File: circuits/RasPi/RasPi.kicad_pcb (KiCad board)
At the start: 2 copper layers, 90 x 57 mm, 276 parts, among them J1 Conn_01x14_Pin, J12 Conn_01x02_MountingPin, J13 Conn_01x03_MountingPin, J14 Conn_01x02_MountingPin, J15 USB_C_Receptacle_USB2.0, J2 Conn_01x06_MountingPin, J3 Conn_01x06_MountingPin, J5 Conn_01x05_Pin, J6 Conn_01x03_MountingPin, J7 RJ45_Hanrun_HR911105A_Horizon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, J8 Conn_01x07_MountingPin, J9 Conn_01x04_MountingPin, Q1 S8550, Q10 BSS138, Q12 SSM6J808R, Q13 BSS138, Q14 SSM6J808R, Q15 S8550, Q16 SSM3J332R, Q17 S8550, Q18 S8550, Q19 S8550, Q2 S8550, Q20 BSS138, Q21 BSS138, Q22 S8550, Q23 BSS138, Q25 BSS138, Q26 SSM3J332R, Q27 BSS138, Q28 SSM3J332R, Q29 BSS138, Q3 S8550, Q30 BSS138, Q33 BSS138, Q4 S8550, Q5 S8550, Q6 SSM3J332R, Q7 S8550, Q8 SSM3J332R, Q9 S8550, SW1 SW_SPST, SW2 SW_DIP_x04, SW3 SW_SPDT, SW4 SW_SPDT_White, SW5 SW_SPDT, SW6 SW_SPDT, SW7 SW_SPST, U1 STM32F446RETx, U10 MAX3485, U11 MAX3485, U12 MAX3485, U13 TPS54560BDDA, U14 MAX3485, U15 STM32H723VGTx, U16 AZ1117CH-3.3, U17 M51957B, U18 DAC_PT8211S, U19 DCDC_TPS61023, U2 MAX3485, U20 FT231XS, U3 MAX3485, U4 MAX3485, U5 MAX3485, U6 SBC_RPi-CM4, U7 FPGA_TangPrimer25K_Core, U8 MAX3485, U9 MAX3485, Y1 16MHz

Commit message: 更新
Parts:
- removed C10: 1uF, Capacitor_SMD:C_0402_1005Metric
- removed C9: 4.7uF, Capacitor_SMD:C_0603_1608Metric
- removed J15: USB_C_Receptacle_USB2.0, Connector_USB:USB_C_Receptacle_G-Switch_GT-USB-7010ASV
- removed L2, L4: 2.2uH, MyLibrary:Inductor_CDPH4D19F
- removed Q29, Q30, Q33: BSS138, Package_TO_SOT_SMD:SOT-23
- removed R3: 10k, Resistor_SMD:R_0402_1005Metric
- removed U20: FT231XS, Package_SO:SSOP-20_3.9x8.7mm_P0.635mm
- added C19: 2.2uF, Capacitor_SMD:C_0402_1005Metric, B.Cu at (-0.40, -13.3)
- added C62: 2.2uF, Capacitor_SMD:C_0402_1005Metric, B.Cu at (14.3, -18.0)
- added C63: 1uF, Capacitor_SMD:C_0402_1005Metric, B.Cu at (5.70, 1.40)
- added J10: USB_C_Receptacle_USB2.0_16P, Connector_USB:USB_C_Receptacle_G-Switch_GT-USB-7010ASV, B.Cu at (40.2, 16.4)
- added J11: Micro_SD_Card_Det_Hirose_DM3AT, TomoshibiLibrary:Connector_SDCard_DM3AT, B.Cu at (-3.39, 17.5)
- added J4: Conn_01x02_Pin, Connector_JST:JST_XH_B2B-XH-AM_1x02_P2.50mm_Vertical, F.Cu at (23.7, 1.80)
- added Q11: 2N7002, Package_TO_SOT_SMD:SOT-23, B.Cu at (68.1, 33.7)
- added Q24: 2N7002, Package_TO_SOT_SMD:SOT-23, B.Cu at (-22.7, 46.9)
- C1, C11, C12, C13, C14, C15, C16, C17, C18, C2, C20, C21, C23, C24, C25, C26, C28, C3, C30, C31, C33, C35, C36, C37, C38, C39, C4, C40, C41, C42, C43, C44, C45, C46, C47, C49, C5, C50, C51, C52, C53, C54, C55, C56, C57, C6, C7, C8, D1, D16, D17, D18, D27, D4, D5, D6, D8, J12, J14, J2, J6, J8, J9, Q1, Q15, Q17, Q18, Q19, Q2, Q22, Q26, Q28, Q3, Q4, Q5, Q6, Q7, Q8, Q9, R1, R10, R102, R103, R104, R105, R106, R107, R108, R109, R11, R110, R111, R112, R113, R114, R117, R119, R12, R120, R121, R122, R13, R14, R15, R16, R17, R18, R19, R2, R20, R21, R22, R23, R24, R25, R26, R27, R28, R29, R30, R31, R32, R33, R34, R35, R36, R37, R38, R39, R4, R40, R41, R44, R45, R46, R47, R48, R49, R5, R50, R53, R54, R55, R56, R57, R58, R59, R6, R60, R61, R62, R63, R64, R65, R66, R67, R68, R69, R7, R70, R71, R72, R73, R74, R75, R76, R77, R78, R79, R8, R80, R81, R82, R83, R84, R85, R86, R87, R88, R89, R9, R90, R91, R92, R93, R94, R95, R96, R97, R98, U10, U11, U12, U13, U14, U15, U16, U17, U18, U19, U2, U3, U4, U5, U8, U9, Y1: moved to B.Cu
- C22: value 1uF -> 0.1uF; moved to B.Cu
- J7: value RJ45_Hanrun_HR911105A_Horizontal -> RJ45_LPJK7001AGNL
- L1: value 22uH -> 1uH; footprint TomoshibiLibrary:Inductor_CDPH4D19F -> Inductor_SMD:L_0603_1608Metric; moved to B.Cu
- Q10, Q13, Q20, Q21, Q23, Q25, Q27: value BSS138 -> 2N7002; moved to B.Cu
- Q12, Q14: footprint TomoshibiLibrary:Package_TSOP6F -> Package_SO:TSOP-6_1.65x3.05mm_P0.95mm
- Q16: value SSM3J332R -> SSM6J808R; footprint Package_TO_SOT_SMD:SOT-23W -> Package_SO:TSOP-6_1.65x3.05mm_P0.95mm; moved to B.Cu
- R100: value 10k -> 1.8k; footprint Resistor_SMD:R_0402_1005Metric -> Resistor_SMD:R_0603_1608Metric; moved to B.Cu
- R99: value 53.6k -> 13k; footprint Resistor_SMD:R_0402_1005Metric -> Resistor_SMD:R_0603_1608Metric; moved to B.Cu
- SW3, SW6: footprint TomoshibiLibrary:SW_Slide_3P_SPDT -> TomoshibiLibrary:SW_Slide_SPDT_SSSS213202
- SW4: value SW_SPDT_White -> SW_SPDT
- U1: value STM32F446RETx -> MODULE_SC0678; footprint Package_QFP:LQFP-64_10x10mm_P0.5mm -> TomoshibiLibrary:SBC_RPi-CM4
- U6: value SBC_RPi-CM4 -> FT231XS; footprint MyLibrary:SBC_RPi-CM4 -> Package_SO:SSOP-20_3.9x8.7mm_P0.635mm
- moved C54 347.9 mm to (-72.3, -32.0)
- moved C53 347.7 mm to (-72.2, -30.2)
- moved U18 347.6 mm to (-70.1, -35.6), turned to 180 degrees
- moved Q21 345.5 mm to (-65.3, 35.7), turned to 180 degrees
- moved R89 341.3 mm to (-62.9, 35.7), turned to -90 degrees
- moved C15 334.7 mm to (-59.4, 35.6), turned to 180 degrees
- moved C16 334.4 mm to (-59.4, 36.6), turned to 180 degrees
- moved C17 334.1 mm to (-59.4, 37.6), turned to 180 degrees
- moved C18 333.8 mm to (-59.4, 38.6), turned to 180 degrees
- moved C26 333.5 mm to (-59.4, 39.6), turned to 180 degrees
- moved R84 328.1 mm to (-46.3, 24.6), turned to 180 degrees
- moved J8 327.8 mm to (-42.4, -3.20), turned to 90 degrees
- moved D23 319.8 mm to (-25.7, 45.0)
- moved D24 318.3 mm to (-25.7, 39.0)
- moved D25 318.1 mm to (-25.7, 40.5)
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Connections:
- net /RingNW/F446RXx_RS485XTX renamed /RingNW/H723RXx_RS485XTX
- net /RingNW/F446RXx_RS485YTX renamed /RingNW/H723RXx_RS485YTX
- net /RingNW/F446TXx_RS485XRX renamed /RingNW/H723TXx_RS485XRX
- net /RingNW/F446TXx_RS485YRX renamed /RingNW/H723TXx_RS485YRX
- C20 pad 1: Net-(C20-Pad1) -> +3.3V
- C22 pad 1: GND -> +3.3V
- C22 pad 2: +3.3V -> GND
- C58 pad 2: GND -> Net-(J10-SHIELD)
- C59 pad 2: GND -> Net-(J10-SHIELD)
- C60 pad 1: GND -> Net-(J10-SHIELD)
- C60 pad 2: Net-(U20-3V3OUT) -> Net-(U6-3V3OUT)
- Q10 pad 1: Net-(D16-K) -> /RingNW/LED_nR0
- Q10 pad 2: Net-(Q10-S) -> GND
- Q10 pad 3: /Power/VSYS -> Net-(D20-A)
- Q13 pad 1: /Power/PowerSW -> /F446RE->RasPi_GPIO3
- Q13 pad 3: Net-(Q13-D) -> /RasPi_GPIO3
- Q16 pad 1: Net-(Q16-G) -> +5V
- Q16 pad 3: /Power/VSYS -> Net-(Q16-G)
- Q20 pad 1: /F446RE->RasPi_GPIO3 -> /ResetIC->RasPi_SHDN
- Q20 pad 3: /RasPi_GPIO3 -> /RasPi_SHDN
- Q23 pad 1: /ResetIC->RasPi_SHDN -> /RasPi_CM4/LED_nR0
- Q23 pad 3: /RasPi_SHDN -> Net-(D29-A)
- R101 pad 1: Net-(U20-USBDP) -> Net-(U6-USBDP)
- R115 pad 1: Net-(U20-USBDM) -> Net-(U6-USBDM)
- R2 pad 1: /RingNW/BOOT -> /RingNW/BOOT0
- R45 pad 1: Net-(Q10-S) -> unconnected-(R45-Pad1)
- R51 pad 1: GND -> Net-(J10-SHIELD)
- R52 pad 1: GND -> Net-(J10-SHIELD)
- R61 pad 2: Net-(Q13-D) -> Net-(Q11-D)
- SW5 pad 1: /RasPi_CM4/GLOBAL_EN -> unconnected-(SW5-A-Pad1)
- SW5 pad 3: unconnected-(SW5-C-Pad3) -> /RasPi_CM4/GLOBAL_EN
- U1 pad 1: +3.3V -> GND
- U1 pad 10: unconnected-(U1-PC2-Pad10) -> /RasPi_CM4/TRD0_N
- U1 pad 12: GND -> /RasPi_CM4/TRD0_P
- U1 pad 13: +3.3V -> GND
- U1 pad 14: unconnected-(U1-PA0-Pad14) -> GND
- U1 pad 15: unconnected-(U1-PA1-Pad15) -> /RasPi_CM4/ETH_LEDY
- U1 pad 17: unconnected-(U1-PA3-Pad17) -> /RasPi_CM4/ETH_LEDG
- U1 pad 18: GND -> unconnected-(U1A-ETHERNET_SYNC_OUT-Pad18)
- U1 pad 19: +3.3V -> unconnected-(U1A-ETHERNET_~{LED1}-Pad19)
- U1 pad 2: unconnected-(U1-PC13-Pad2) -> GND
- U1 pad 21: unconnected-(U1-PA5-Pad21) -> /RasPi_CM4/LED_nACT
- U1 pad 22: unconnected-(U1-PA6-Pad22) -> GND
- U1 pad 23: unconnected-(U1-PA7-Pad23) -> GND
- U1 pad 25: unconnected-(U1-PC5-Pad25) -> /PCM_DOUT
- U1 pad 26: unconnected-(U1-PB0-Pad26) -> /PCM_FS
- U1 pad 27: unconnected-(U1-PB1-Pad27) -> /PCM_DIN
- U1 pad 28: Net-(U1-PB2) -> unconnected-(U1A-GPIO13-Pad28)
- U1 pad 30: Net-(U1-VCAP_1) -> unconnected-(U1A-GPIO6-Pad30)
- U1 pad 31: GND -> unconnected-(U1A-GPIO12-Pad31)
- U1 pad 32: +3.3V -> GND
- U1 pad 33: unconnected-(U1-PB12-Pad33) -> GND
- U1 pad 4: unconnected-(U1-PC15-Pad4) -> /RasPi_CM4/TRD1_P
- U1 pad 42: unconnected-(U1-PA9-Pad42) -> GND
- U1 pad 43: unconnected-(U1-PA10-Pad43) -> GND
- U1 pad 46: /RingNW/SWDIO -> unconnected-(U1A-GPIO22-Pad46)
- U1 pad 47: GND -> unconnected-(U1A-GPIO23-Pad47)
- U1 pad 48: +3.3V -> unconnected-(U1A-GPIO27-Pad48)
- U1 pad 49: /RingNW/SWCLK -> /PCM_CLK
- U1 pad 5: /RingNW/HSE_IN -> unconnected-(U1A-ETHERNET_PAIR3_N-Pad5)
- U1 pad 51: unconnected-(U1-PC10-Pad51) -> /RasPi_CM4/RasPiRX0_SerialTX
- U1 pad 52: unconnected-(U1-PC11-Pad52) -> GND
- U1 pad 53: unconnected-(U1-PC12-Pad53) -> GND
- U1 pad 55: /RingNW/SWO -> /RasPi_CM4/RasPiTX0_SerialRX
- U1 pad 56: unconnected-(U1-PB4-Pad56) -> /RasPi_GPIO3
- U1 pad 57: unconnected-(U1-PB5-Pad57) -> /RasPi_CM4/SD_CLK
- U1 pad 59: unconnected-(U1-PB7-Pad59) -> GND
- U1 pad 6: /RingNW/HSE_OUT -> /RasPi_CM4/TRD1_N
- U1 pad 60: /RingNW/BOOT -> GND
- U1 pad 61: unconnected-(U1-PB8-Pad61) -> /RasPi_CM4/SD_DAT3
- U1 pad 62: unconnected-(U1-PB9-Pad62) -> /RasPi_CM4/SD_CMD
- U1 pad 63: GND -> /RasPi_CM4/SD_DAT0
- U1 pad 64: +3.3V -> unconnected-(U1A-SD_DAT5-Pad64)
- U1 pad 7: /RingNW/NRST -> GND
- U1 pad 8: unconnected-(U1-PC0-Pad8) -> GND
- U15 pad 20: unconnected-(U15-VREF+-Pad20) -> +3.3V
- U15 pad 48: unconnected-(U15-VCAP-Pad48) -> Net-(C19-Pad1)
- U15 pad 72: unconnected-(U15-PA13(JTMS-Pad72) -> /RingNW/SWDIO
- U15 pad 73: Net-(C20-Pad1) -> Net-(C62-Pad1)
- U15 pad 76: unconnected-(U15-PA14(JTCK-Pad76) -> /RingNW/SWCLK
- U15 pad 89: unconnected-(U15-PB3(JTDO-Pad89) -> /RingNW/SWO
- U15 pad 94: /RingNW/BOOT -> /RingNW/BOOT0
- U6 pad 1: GND -> unconnected-(U6-~{DTR}-Pad1)
- U6 pad 11: unconnected-(U6A-ETHERNET_PAIR2_P-Pad11) -> Net-(U6-USBDP)
- U6 pad 12: unconnected-(U6A-ETHERNET_PAIR0_P-Pad12) -> Net-(U6-USBDM)
- U6 pad 13: GND -> Net-(U6-3V3OUT)
- U6 pad 14: GND -> Net-(U6-3V3OUT)
- U6 pad 15: unconnected-(U6A-ETHERNET_~{LED3}-Pad15) -> VBUS
- U6 pad 16: unconnected-(U6A-ETHERNET_SYNC_IN-Pad16) -> GND
- U6 pad 2: GND -> unconnected-(U6-~{RTS}-Pad2)
- U6 pad 20: unconnected-(U6A-EEPROM_~{WP}-Pad20) -> /RasPi_CM4/RasPiRX0_SerialTX
- U6 pad 3: unconnected-(U6A-ETHERNET_PAIR3_P-Pad3) -> Net-(U6-3V3OUT)
- U6 pad 4: unconnected-(U6A-ETHERNET_PAIR1_P-Pad4) -> /RasPi_CM4/RasPiTX0_SerialRX
- U6 pad 6: unconnected-(U6A-ETHERNET_PAIR1_N-Pad6) -> Net-(J10-SHIELD)
- U6 pad 7: GND -> unconnected-(U6-~{DSR}-Pad7)
- U6 pad 8: GND -> unconnected-(U6-~{DCD}-Pad8)
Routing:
- net /RasPi_CM4/TRD1_N: track 0.00 -> 55.1 mm
- net /RasPi_CM4/TRD1_P: track 0.00 -> 55.0 mm
- net /RasPi_CM4/TRD0_P: track 0.00 -> 51.3 mm
- net /RasPi_CM4/TRD0_N: track 0.00 -> 51.3 mm
- net unconnected-(U7-B10_IOL12B-PadB57): track 0.00 -> 45.8 mm
- net unconnected-(U7-B11_IOL12A-PadB55): track 0.00 -> 44.4 mm
- net unconnected-(U7-C11_IOL5A-PadB51): track 0.00 -> 41.8 mm
- net +3.3V: track 0.00 -> 28.6 mm
- net /FPGA_TangPrimerCore/RS485_Panel/RS485_Panel0: track 0.00 -> 26.4 mm
- net /FPGA_TangPrimerCore/RS485_Panel/RS485_Panel1: track 0.00 -> 22.2 mm
- net /DSI_D1_P: track 0.00 -> 21.4 mm, vias 0 -> 2
- net /DSI_D1_N: track 0.00 -> 21.4 mm, vias 0 -> 2
- net /DSI_D0_P: track 0.00 -> 21.3 mm, vias 0 -> 2
- net /DSI_CK_N: track 0.00 -> 21.2 mm, vias 0 -> 2
- net /DSI_D0_N: track 0.00 -> 21.2 mm, vias 0 -> 2
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- added copper zone on In1.Cu, net GND
- added copper zone on In2.Cu, net GND
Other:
- outline, holes or cut-outs redrawn
- copper layers 2 -> 4
- board text added: "3.3V"
- board text added: "5VDCDC"
- board text added: "表：放電 裏：昇圧"

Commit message: raspi基板回路図
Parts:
- removed J8: Conn_01x07_MountingPin, Connector_Molex:Molex_PicoBlade_53261-0771_1x07-1MP_P1.25mm_Horizontal
- added C10: 10uF, Capacitor_SMD:C_1206_3216Metric, B.Cu at (53.5, 13.7)
- added C64: 22uF, Capacitor_SMD:C_0805_2012Metric, F.Cu at (64.5, 55.8)
- added C65: 4.7nF, Capacitor_SMD:C_0402_1005Metric, F.Cu at (64.3, 48.6)
- added C66: 100uF, Capacitor_SMD:C_1206_3216Metric, F.Cu at (64.3, 51.1)
- added C67: 100uF, Capacitor_SMD:C_1206_3216Metric, F.Cu at (-40.8, 49.8)
- added C68: 10uF, Capacitor_SMD:C_0805_2012Metric, F.Cu at (-35.7, 54.2)
- added C70: 15pF, Capacitor_SMD:C_0402_1005Metric, F.Cu at (-31.3, 49.1)
- added C9: 100uF, Capacitor_SMD:C_1206_3216Metric, B.Cu at (53.1, 26.6)
- added D19: Blue, LED_SMD:LED_0603_1608Metric_Pad1.05x0.95mm_HandSolder, F.Cu at (22.7, -18.2)
- added D28: Blue, LED_SMD:LED_0603_1608Metric_Pad1.05x0.95mm_HandSolder, F.Cu at (22.7, -16.7)
- added H1: MountingHole_Pad, TestPoint:TestPoint_Pad_1.0x1.0mm, F.Cu at (-40.4, -3.50)
- added H2: MountingHole_Pad, TestPoint:TestPoint_Pad_1.0x1.0mm, F.Cu at (-40.4, -1.90)
- added H3: MountingHole_Pad, TestPoint:TestPoint_Pad_1.0x1.0mm, F.Cu at (-40.4, -0.30)
- added H4: MountingHole_Pad, TestPoint:TestPoint_Pad_1.0x1.0mm, F.Cu at (-40.4, 1.30)
- added H5: MountingHole_Pad, TestPoint:TestPoint_Pad_1.0x1.0mm, F.Cu at (57.1, -27.8)
- added H6: MountingHole_Pad, TestPoint:TestPoint_Pad_1.0x1.0mm, F.Cu at (57.1, -24.2)
- added H7: MountingHole_Pad, TestPoint:TestPoint_Pad_1.0x1.0mm, F.Cu at (32.3, -44.2)
- added H8: MountingHole_Pad, TestPoint:TestPoint_Pad_1.0x1.0mm, F.Cu at (32.4, -40.2)
- added J15: Conn_01x08_MountingPin, Connector_Molex:Molex_PicoBlade_53261-0871_1x08-1MP_P1.25mm_Horizontal, B.Cu at (-42.4, -3.00)
- added L2: 3.3uH, TomoshibiLibrary:Inductor_ECS-MPIL0530, B.Cu at (63.5, 19.9)
- added L4: 1uH, Inductor_SMD:L_1210_3225Metric, F.Cu at (-40.8, 53.5)
- added Q29: SSM6J808R, Package_SO:TSOP-6_1.65x3.05mm_P0.95mm, F.Cu at (57.7, -3.65)
- added R116: 22k, Resistor_SMD:R_0402_1005Metric, F.Cu at (67.8, 45.8)
- added R118: 5.1k, Resistor_SMD:R_0603_1608Metric, F.Cu at (-33.1, 42.8)
- added R123: 2k, Resistor_SMD:R_0603_1608Metric, F.Cu at (-33.1, 45.3)
- added R124: 100k, Resistor_SMD:R_0402_1005Metric, F.Cu at (-32.0, 53.7)
- added R3: 1k, Resistor_SMD:R_0402_1005Metric, B.Cu at (29.7, -32.4)
- added R42: 1k, Resistor_SMD:R_0402_1005Metric, B.Cu at (29.7, -30.9)
- added R43: 2k, Resistor_SMD:R_0402_1005Metric, B.Cu at (66.3, 24.4)
- added U20: M51957B, Package_SO:SOP-8_3.9x4.9mm_P1.27mm, F.Cu at (-39.4, 44.9)
- added U21: 74AHC1G02, Package_TO_SOT_SMD:SOT-23-5, F.Cu at (-35.4, 50.5)
- C15: value 0.1uF -> 1uF
- C16, C17: value 0.1uF -> 10uF; footprint Capacitor_SMD:C_0402_1005Metric -> Capacitor_SMD:C_1206_3216Metric
- C18, C26: value 0.1uF -> 100uF; footprint Capacitor_SMD:C_0402_1005Metric -> Capacitor_SMD:C_1206_3216Metric
- C47: value 4700pF -> 15pF; footprint Capacitor_SMD:C_0603_1608Metric -> Capacitor_SMD:C_0402_1005Metric
- C49: footprint Capacitor_SMD:C_0805_2012Metric -> Capacitor_SMD:C_1206_3216Metric
- C50: value 47uF -> 15pF; footprint Capacitor_SMD:C_0805_2012Metric -> Capacitor_SMD:C_0402_1005Metric; moved to F.Cu
- C51, C54: footprint Capacitor_SMD:C_0603_1608Metric -> Capacitor_SMD:C_0402_1005Metric
- C53: value 47uF -> 22uF
- C55: value 47uF -> 10uF
- C56: value 1uF -> 0.1uF; footprint Capacitor_SMD:C_0603_1608Metric -> Capacitor_SMD:C_0402_1005Metric
- C57: value 47uF -> 10nF; footprint Capacitor_SMD:C_0805_2012Metric -> Capacitor_SMD:C_0402_1005Metric
- D17: value SS2040FL -> MA10EB045; footprint Diode_SMD:D_SOD-123 -> Diode_SMD:Vishay_SMPA
- R119: value 200k -> 100k
- R121: value 53.6k -> 22k
- R122: value 10k -> 2.2k
- R54: value 75k -> 100k
- R57: value 5.1k -> 7.5k
- SW4: footprint TomoshibiLibrary:SW_Slide_SPDT_White -> TomoshibiLibrary:SW_Slide_SPDT_IS-1235-G
- U1: value MODULE_SC0678 -> SBC_RPi-CM4
- moved C16 114.8 mm to (53.5, 15.8)
- moved C17 114.6 mm to (53.5, 17.9)
- moved C18 113.7 mm to (53.1, 22.4)
- moved C26 113.5 mm to (53.1, 24.5)
- moved Q23 96.4 mm to (32.7, -35.4)
- moved Q24 96.4 mm to (32.7, -32.0)
- moved R110 96.4 mm to (35.1, -32.0)
- moved R111 96.4 mm to (29.7, -39.9)
- moved R112 96.4 mm to (29.7, -38.4)
- moved R113 96.4 mm to (29.7, -33.9)
- moved R114 96.4 mm to (29.7, -36.9)
- moved R117 96.4 mm to (35.1, -35.4)
- moved R120 96.4 mm to (29.7, -35.4)
- moved U18 94.8 mm to (24.4, -42.7), turned to 90 degrees
- moved C54 94.0 mm to (20.8, -44.9), turned to -90 degrees
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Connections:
- net /F446RE->RasPi_GPIO3 renamed /MCU->RasPi_GPIO3
- net /RasPi->RST_TangPrimer renamed /RasPi->RST_FPGA
- C16 pad 1: +5V -> VCC
- C17 pad 1: +5V -> VCC
- C18 pad 1: +5V -> /Power/VSYS
- C26 pad 1: +5V -> /Power/VSYS
- C47 pad 1: GND -> (no net)
- C47 pad 2: Net-(U17-Cdelay) -> GND
- C50 pad 1: VCC -> (no net)
- C55 pad 1: /Power/Cap -> GND
- C55 pad 2: GND -> /Power/Cap
- C56 pad 1: /Power/VSYS -> GND
- C56 pad 2: GND -> +5V
- C57 pad 2: GND -> /Power/FB_Boost
- C58 pad 2: Net-(J10-SHIELD) -> GND
- C59 pad 2: Net-(J10-SHIELD) -> GND
- C60 pad 1: Net-(J10-SHIELD) -> GND
- J10 pad A1: Net-(J10-SHIELD) -> GND
- J10 pad A12: Net-(J10-SHIELD) -> GND
- J10 pad B1: Net-(J10-SHIELD) -> GND
- J10 pad B12: Net-(J10-SHIELD) -> GND
- J10 pad S1: Net-(J10-SHIELD) -> GND
- J9 pad 3: /RasPi_CM4/RasPiTXx_LiDARRX -> /RasPi_CM4/RasPiTX5_LiDARRX
- J9 pad 4: /RasPi_CM4/RasPiRXx_LiDARTX -> /RasPi_CM4/RasPiRX5_LiDARTX
- Q21 pad 3: /RST_TangPrimer -> /RST_FPGA
- R122 pad 1: GND -> Net-(R122-Pad1)
- R122 pad 2: /Power/FB_Buck -> GND
- R45 pad 1: unconnected-(R45-Pad1) -> Net-(Q29-D-Pad1)
- R51 pad 1: Net-(J10-SHIELD) -> GND
- R52 pad 1: Net-(J10-SHIELD) -> GND
- R92 pad 1: +3.3V -> CM4_3.3V(OUTPUT)__1
- U1 pad 28: unconnected-(U1A-GPIO13-Pad28) -> /RasPi_CM4/RasPiRX5_LiDARTX
- U1 pad 30: unconnected-(U1A-GPIO6-Pad30) -> /RasPi->FPGA_MOSI
- U1 pad 31: unconnected-(U1A-GPIO12-Pad31) -> /RasPi_CM4/RasPiTX5_LiDARRX
- U1 pad 34: unconnected-(U1A-GPIO5-Pad34) -> /RasPi->FPGA_MISO
- U1 pad 37: unconnected-(U1A-GPIO7-Pad37) -> /RasPi->FPGA_SCLK
- U1 pad 38: unconnected-(U1A-GPIO11-Pad38) -> /RasPi->MCU_SCLK
- U1 pad 39: unconnected-(U1A-GPIO8-Pad39) -> /RasPi->MCU_CS
- U1 pad 40: unconnected-(U1A-GPIO9-Pad40) -> /RasPi->MCU_MISO
- U1 pad 44: unconnected-(U1A-GPIO10-Pad44) -> /RasPi->MCU_MOSI
- U1 pad 54: unconnected-(U1A-GPIO4-Pad54) -> /RasPi->FPGA_CS
- U1 pad 80: unconnected-(U1A-SCL0-Pad80) -> /RasPi_CM4/LiDAR_PWM
- U13 pad 6: unconnected-(U13-COMP-Pad6) -> Net-(U13-COMP)
- U19 pad 2: /Power/VSYS -> /Power/EN_Boost
- U19 pad 3: /Power/VSYS -> /Power/Cap
- U6 pad 6: Net-(J10-SHIELD) -> GND
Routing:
- net (no net): track 0.00 -> 171.2 mm, vias 0 -> 22
- net GND: track 8.63 -> 94.2 mm, vias 12 -> 16
- net +3.3V: track 28.6 -> 86.8 mm
- net unconnected-(U7-A11_IOL14A-PadB56): track 0.00 -> 42.6 mm
- net /PCM_CLK: track 0.00 -> 41.2 mm
- net unconnected-(U7-E10_IOL3B-PadB54): track 0.00 -> 38.9 mm
- net /PCM_DIN: track 0.00 -> 37.7 mm
- net unconnected-(U7-E11_IOL3A-PadB52): track 0.00 -> 37.6 mm
- net /RasPi->FPGA_SCLK: track 0.00 -> 36.0 mm, vias 0 -> 2
- net /PCM_DOUT: track 0.00 -> 35.7 mm
- net /RasPi->FPGA_CS: track 0.00 -> 34.7 mm, vias 0 -> 2
- net unconnected-(U7-L11_IOT11B-PadB48): track 0.00 -> 34.2 mm
- net /PCM_FS: track 0.00 -> 34.1 mm, vias 0 -> 1
- net /RasPi->FPGA_MISO: track 0.00 -> 32.9 mm, vias 0 -> 2
- net /RasPi_CM4/SD_DAT3: track 0.00 -> 32.1 mm, vias 0 -> 2
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- added copper zone on B.Cu, net +3.3V

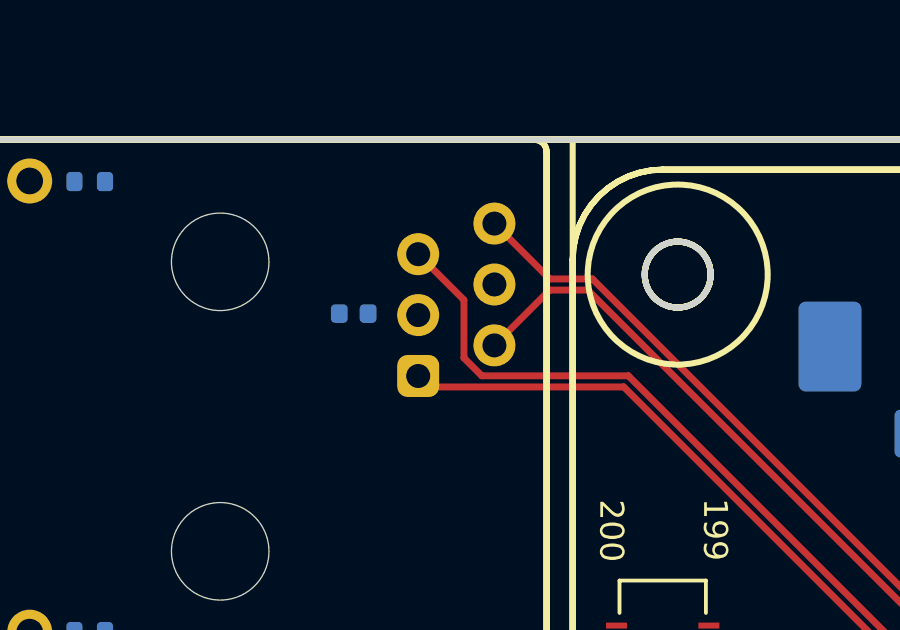
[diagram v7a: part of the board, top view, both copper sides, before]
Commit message: 発注_第一弾
Drive, 1stLayer_Power, 2ndLayer_3rdLayer
を発注
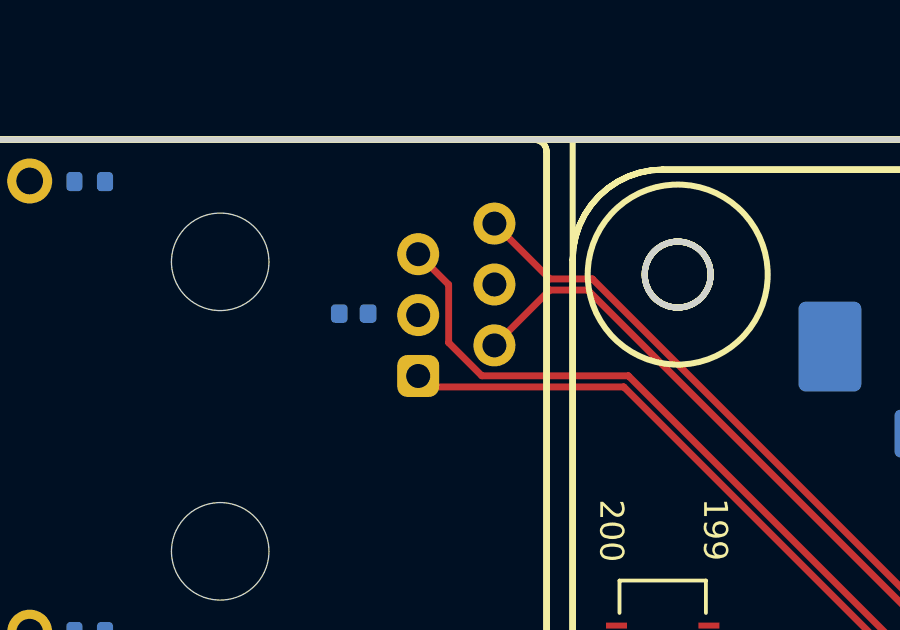
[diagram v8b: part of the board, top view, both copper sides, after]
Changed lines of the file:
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@@
   (segment (start -24.78502 -20.25502) (end -18.296649 -20.25502) (width 0.23) (layer "F.Cu") (net 359))
   (segment (start -18.296649 -20.25502) (end 8.823371 6.865) (width 0.23) (layer "F.Cu") (net 359))
+  (segment (start -24.135 -21.729573) (end -23.030447 -20.62502) (width 0.23) (layer "F.Cu") (net 360))
+  (segment (start -24.135 -23.665) (end -24.135 -21.729573) (width 0.23) (layer "F.Cu") (net 360))
+  (segment (start 8.976631 6.495) (end 14.67 6.495) (width 0.23) (layer "F.Cu") (net 360))
+  (segment (start -23.030447 -20.62502) (end -18.143389 -20.62502) (width 0.23) (layer "F.Cu") (net 360))
   (segment (start -18.143389 -20.62502) (end 8.976631 6.495) (width 0.23) (layer "F.Cu") (net 360))
-  (segment (start -23.625 -21.219573) (end -23.030447 -20.62502) (width 0.23) (layer "F.Cu") (net 360))
-  (segment (start 8.976631 6.495) (end 14.67 6.495) (width 0.23) (layer "F.Cu") (net 360))
-  (segment (start -25.15 -24.68) (end -23.625 -23.155) (width 0.23) (layer "F.Cu") (net 360))
-  (segment (start -23.030447 -20.62502) (end -18.143389 -20.62502) (width 0.23) (layer "F.Cu") (net 360))
-  (segment (start -23.625 -23.155) (end -23.625 -21.219573) (width 0.23) (layer "F.Cu") (net 360))
+  (segment (start -25.15 -24.68) (end -24.135 -23.665) (width 0.23) (layer "F.Cu") (net 360))
   (segment (start -20.765 -23.485) (end -19.49663 -23.485) (width 0.23) (layer "F.Cu") (net 361))
   (segment (start 9.67837 5.69) (end 14.89 5.69) (width 0.23) (layer "F.Cu") (net 361))
